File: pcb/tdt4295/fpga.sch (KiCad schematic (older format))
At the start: 43 parts, among them J101 FPGA__debug, J102 Conn_01x02, U101 S25FL127SABMFV101, U102 XC7A100T-FTG256-tdt4295

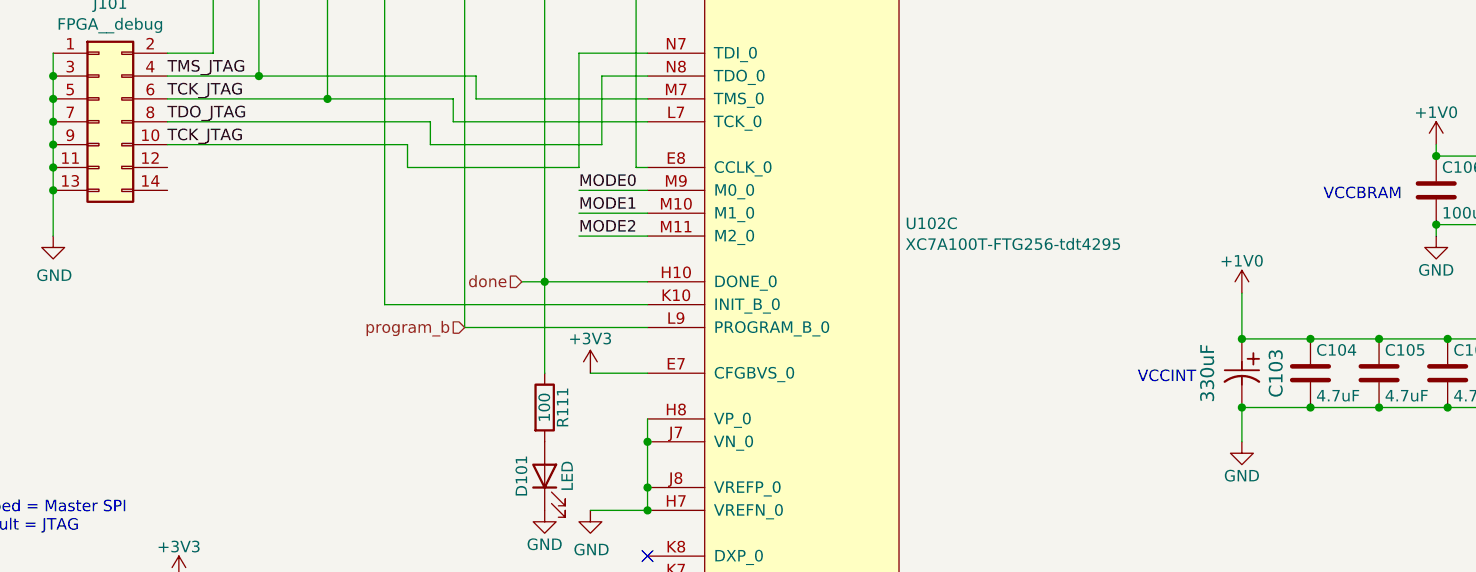
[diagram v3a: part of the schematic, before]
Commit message: Add some no connection symbols
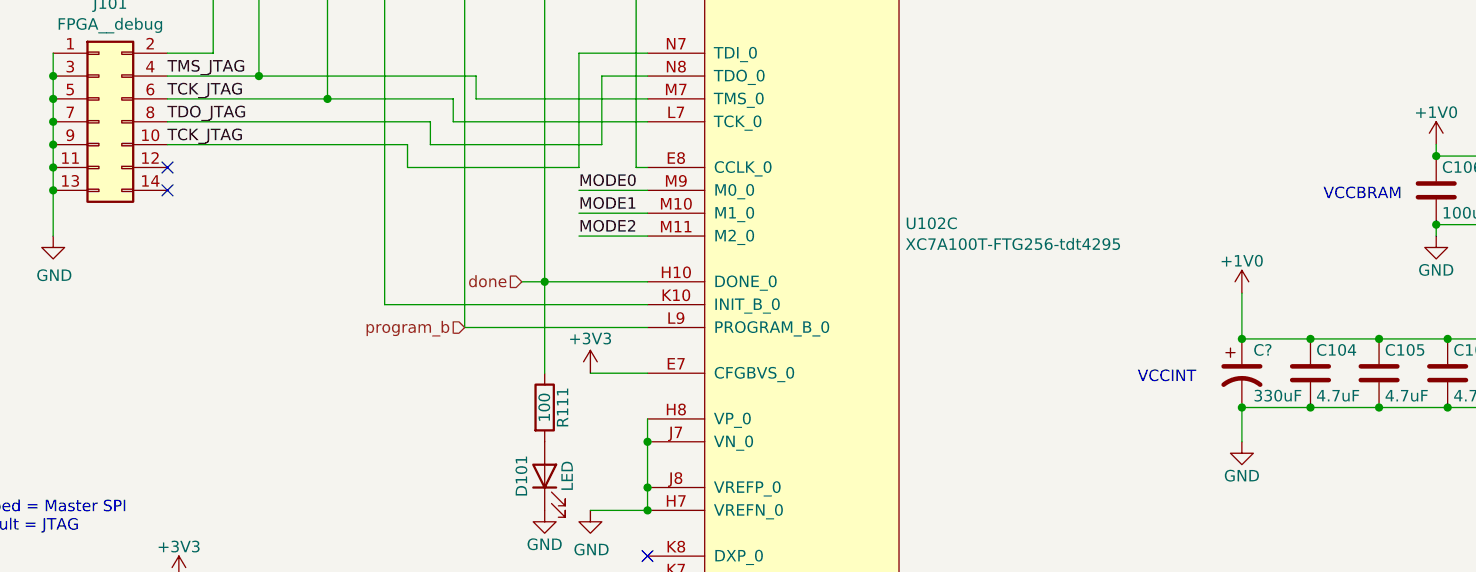
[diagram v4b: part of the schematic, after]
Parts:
- removed C103: 330uF, T520V337M2R5ATE025-footprint:T520V337M2R5ATE025, symbol T520V337M2R5ATE025:T520V337M2R5ATE025
- added C?: 330uF, symbol Device:CP1
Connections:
- net +1V0: now also C?.1
- net GND: now also C?.2
- no-connect marks 2 -> 4
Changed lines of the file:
@@
 Wire Wire Line
 	6600 6400 6600 6550
-Connection ~ 6600 6400
 Connection ~ 6900 6400
 Wire Wire Line
@@
 Wire Wire Line
 	6600 6100 6600 5900
-Connection ~ 6600 6100
 Connection ~ 6900 6100
 Wire Wire Line
@@
 Text Notes 7300 5500 2    50   ~ 0
 VCCBRAM
-$Comp
-L T520V337M2R5ATE025:T520V337M2R5ATE025 C103
-U 1 1 614CD791
-P 6600 6100
-F 0 "C103" H 6750 6250 60  0000 C CNN
-F 1 "330uF" H 6750 5950 60  0000 C CNN
-F 2 "T520V337M2R5ATE025-footprint:T520V337M2R5ATE025" H 6750 5740 60  0001 C CNN
-F 3 "" H 6600 6100 60  0000 C CNN
-F 4 "T520V337M2R5ATE025" H 6600 6100 50  0001 C CNN "Component name"
-	1    6600 6100
-	0    1    1    0
-$EndComp
 $Comp
 L Device:R R111
@@
 	1    0    0    -1
 $EndComp
+$Comp
+L Device:CP1 C?
+U 1 1 614EBAD6
+P 6600 6250
+F 0 "C?" H 6650 6350 50  0000 L CNN
+F 1 "330uF" H 6650 6150 50  0000 L CNN
+F 2 "" H 6600 6250 50  0001 C CNN
+F 3 "~" H 6600 6250 50  0001 C CNN
+	1    6600 6250
+	1    0    0    -1
+$EndComp
+Connection ~ 6600 6100
+Connection ~ 6600 6400
+NoConn ~ 1900 5350
+NoConn ~ 1900 5450
 $EndSCHEMATC

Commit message: annotation fix
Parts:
- gave numbers to parts that had none: 1
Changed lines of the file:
@@
 	8850 2250 8900 2250
-Wire Wire Line
-	8850 1650 8850 2150
 Wire Wire Line
 	8900 1650 8850 1650
@@
 	10900 2350 10900 2250
 Connection ~ 10900 2350
-Wire Wire Line
-	10900 2250 10900 2150
 Connection ~ 10900 2250
 $Comp
@@
 	10900 950  10900 800
 Connection ~ 10900 950
-Wire Wire Line
-	10900 1550 10900 1450
 $Comp
 L xc7a100t-ftg256-modified:XC7A100T-FTG256-tdt4295 U102
@@
 $EndComp
 $Comp
-L Device:CP1 C?
+L Device:CP1 C103
 U 1 1 614EBAD6
 P 6600 6250
-F 0 "C?" H 6650 6350 50  0000 L CNN
+F 0 "C103" H 6650 6350 50  0000 L CNN
 F 1 "330uF" H 6650 6150 50  0000 L CNN
 F 2 "" H 6600 6250 50  0001 C CNN
@@
 NoConn ~ 1900 5350
 NoConn ~ 1900 5450
+Wire Wire Line
+	8850 1650 8850 2150
+Wire Wire Line
+	10900 2150 10900 2250
+Wire Wire Line
+	10900 1450 10900 1550
 $EndSCHEMATC

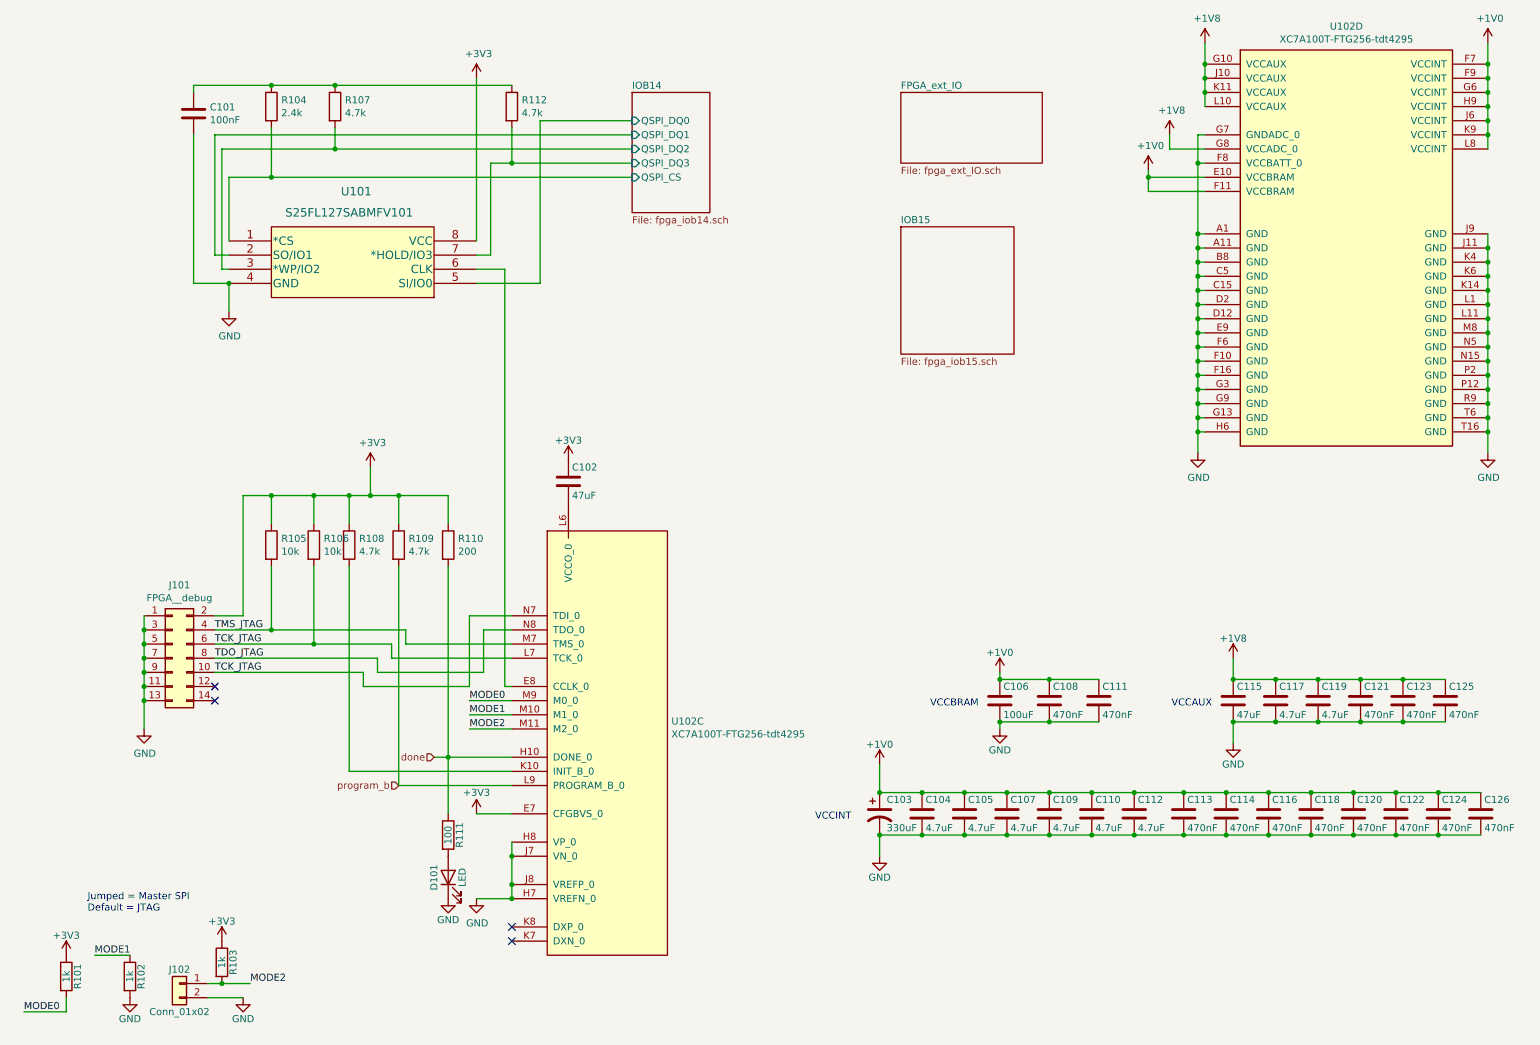
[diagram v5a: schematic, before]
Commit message: correct errors spotted by Markus
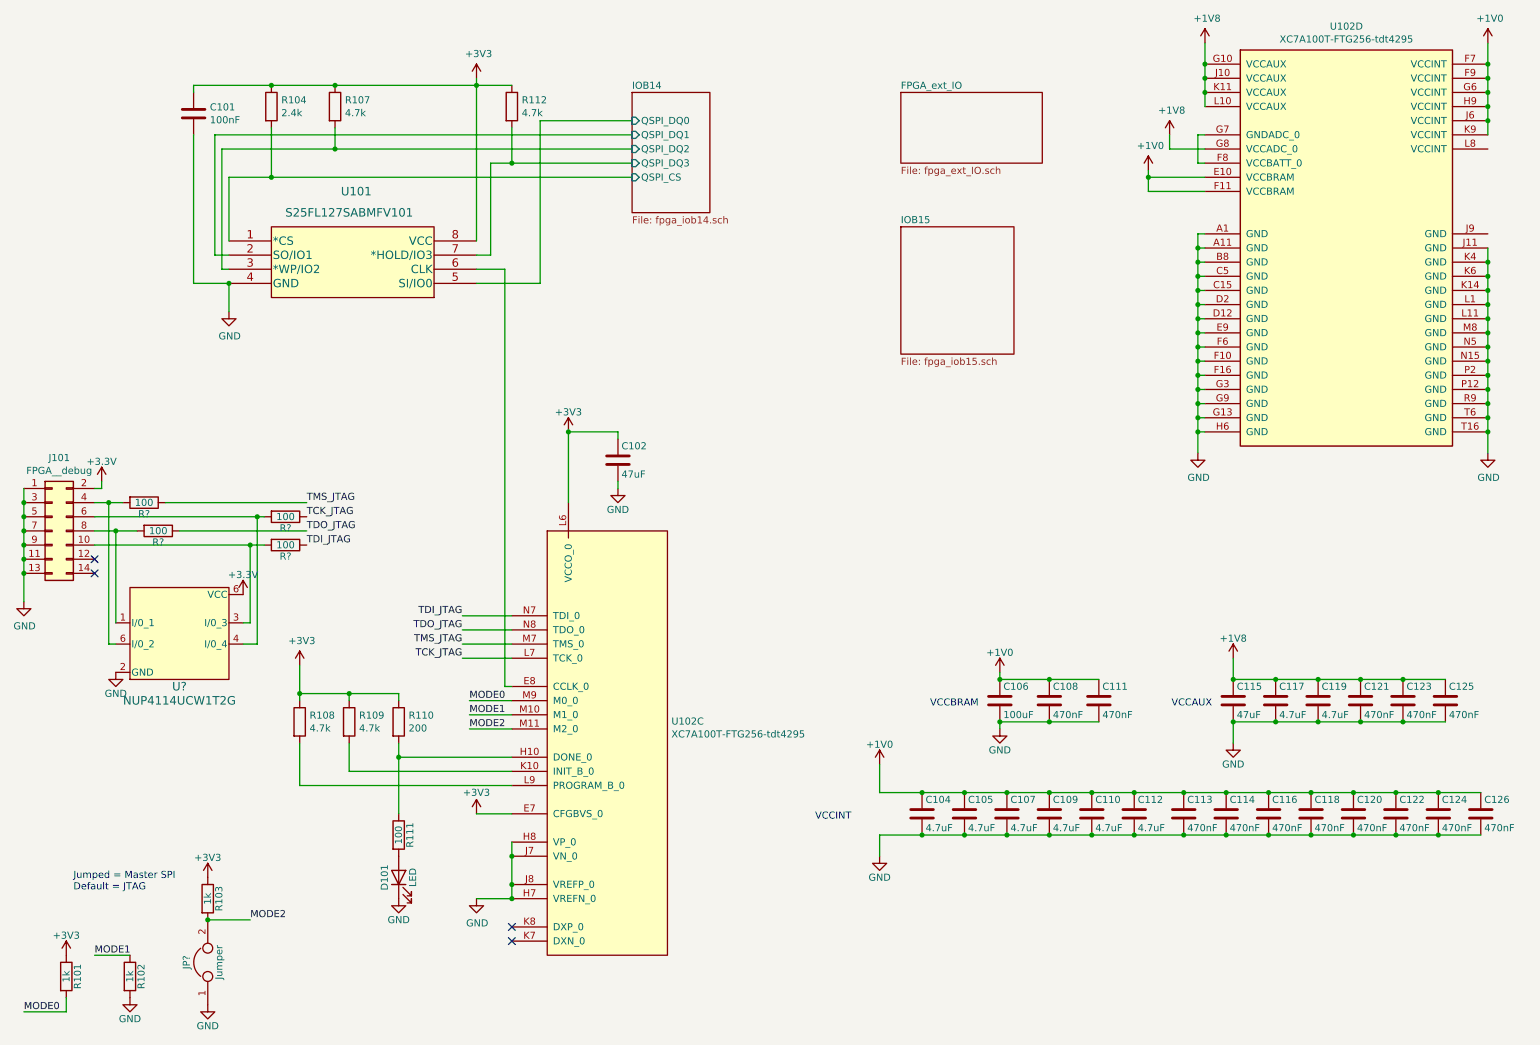
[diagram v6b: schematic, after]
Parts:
- removed C103: 330uF, symbol Device:CP1
- removed J102: Conn_01x02, Connector_PinHeader_2.54mm:PinHeader_1x02_P2.54mm_Vertical, symbol Connector_Generic:Conn_01x02
- removed R105, R106: 10k, Resistor_SMD:R_0805_2012Metric_Pad1.20x1.40mm_HandSolder, symbol Device:R
- added JP?: Jumper, Connector_PinSocket_2.54mm:PinSocket_1x02_P2.54mm_Vertical, symbol Device:Jumper
- added R? (x4): 100, symbol Device:R
- added U?: NUP4114UCW1T2G, SOIC_W1T2G_ONS, symbol NUP4114UCW1T2G:NUP4114UCW1T2G
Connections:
- net +1V0: no longer U102.L8 (VCCINT)
- net +3V3: now also C101.1, R104.1, R107.1, R112.1, U102.L6 (VCCO_0), U?.6 (VCC)
- net GND: now also C102.2, JP?.1, U?.2 (GND); no longer U102.F8 (VCCBATT_0), U102.G7 (GNDADC_0), U102.J9 (GND)
- net MODE2: now also JP?.2
- net TCK_JTAG: now also R?.1; no longer J101.10 (Pin_10), J101.6 (Pin_6), U102.N7 (TDI_0)
- net TDO_JTAG: now also R?.1; no longer J101.8 (Pin_8)
- net TMS_JTAG: now also R?.1; no longer J101.4 (Pin_4)
- net at U102.K10 (INIT_B_0): now also R109.2; no longer R108.2
- net done: no longer names the net of R110.2, R111.1, U102.H10 (DONE_0)
- net program_b: no longer names the net of U102.L9 (PROGRAM_B_0)
- net program_b: now also R108.2; no longer R109.2
- new net: J101.10 (Pin_10), R?.2, U?.3 (I/0_3)
- new net: J101.4 (Pin_4), R?.2, U?.6 (VCC)
- new net: J101.6 (Pin_6), R?.2, U?.4 (I/0_4)
- new net: J101.8 (Pin_8), R?.2, U?.1 (I/0_1)
- new net: U102.F8 (VCCBATT_0), U102.G7 (GNDADC_0)
- new net TDI_JTAG: R?.1, U102.N7 (TDI_0)
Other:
- moved on the sheet: C102, D101, J101, R103, R108, R109, R110, R111
